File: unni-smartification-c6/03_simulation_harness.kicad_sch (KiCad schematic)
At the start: 10 parts

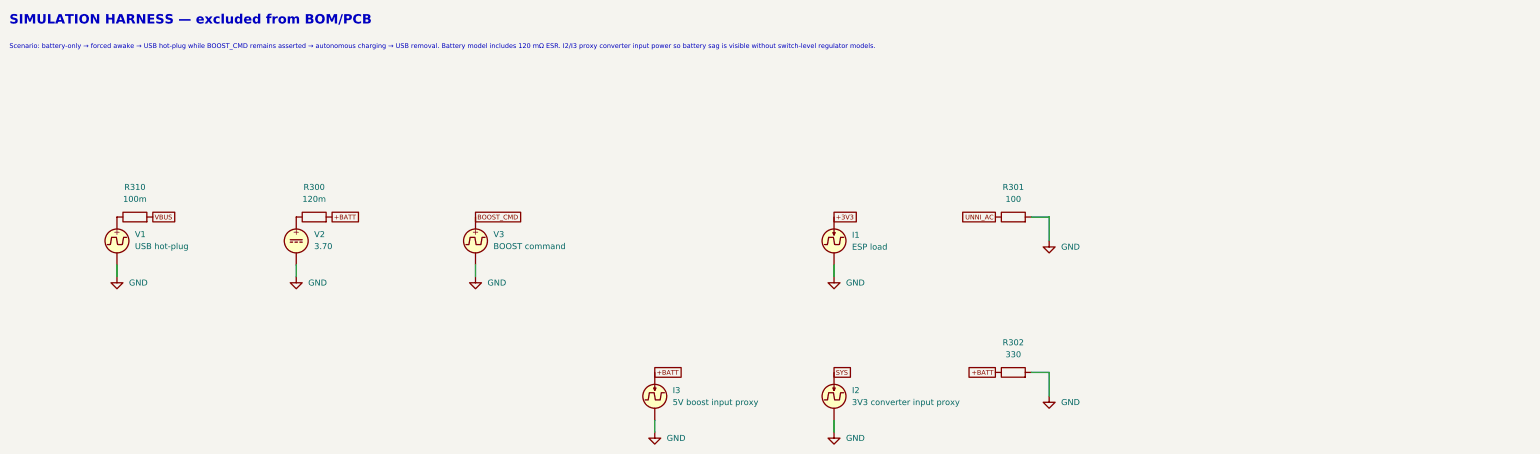
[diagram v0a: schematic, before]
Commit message: Validate power paths and fix KiCad SPICE models
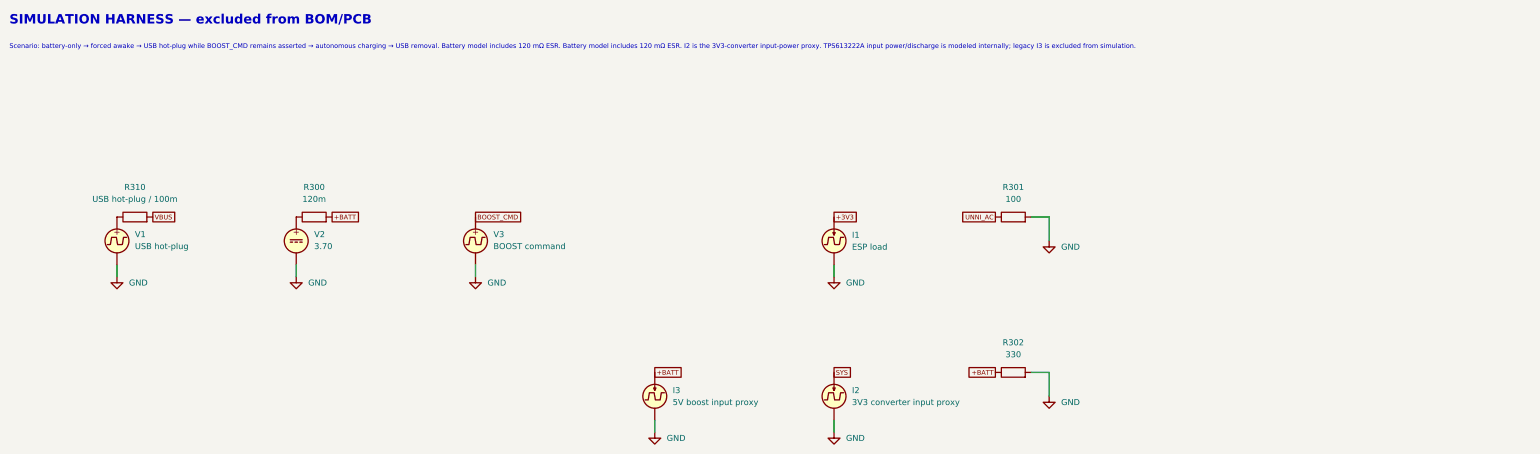
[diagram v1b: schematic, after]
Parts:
- R310: value 100m -> USB hot-plug / 100m
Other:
- note added: "Scenario: battery-only → forced awake → USB hot-plug while BOOST_CMD remains asserted → autonomous charging → USB removal. Battery model includes 120 mΩ ESR. Battery model includes 120 mΩ ESR. I2 is the 3V3-converter input-power proxy. TPS613222A input power/discharge is modeled internally; legacy I3 is excluded from simulation."
- note removed: "Scenario: battery-only → forced awake → USB hot-plug while BOOST_CMD remains asserted → autonomous charging → USB removal. Battery model includes 120 mΩ ESR. I2/I3 proxy converter input power so battery sag is visible without switch-level regulator models."
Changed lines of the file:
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@@
 		(title "Simulation Harness")
 		(date "2026-08-19")
-		(rev "A-v28-final")
+		(rev "A-v29-validated")
 		(company "Unni CO2 Smartification")
 	)
@@
 		)
 	)
-	(text "Scenario: battery-only → forced awake → USB hot-plug while BOOST_CMD remains asserted → autonomous charging → USB removal. Battery model includes 120 mΩ ESR. I2/I3 proxy converter input power so battery sag is visible without switch-level regulator models."
+	(text "Scenario: battery-only → forced awake → USB hot-plug while BOOST_CMD remains asserted → autonomous charging → USB removal. Battery model includes 120 mΩ ESR. Battery model includes 120 mΩ ESR. I2 is the 3V3-converter input-power proxy. TPS613222A input power/discharge is modeled internally; legacy I3 is excluded from simulation."
 		(exclude_from_sim no)
 		(at 15.24 20.32 0)
@@
 			)
 		)
-		(property "Value" "100m"
+		(property "Value" "USB hot-plug / 100m"
 			(at 41.91 52.07 90)
 			(show_name no)
@@
 			)
 		)
-		(property "Description" "USB source/cable resistance (simulation only)"
+		(property "Description" "USB hot-plug switch with 100m on-resistance (simulation only)"
 			(at 41.91 55.88 0)
 			(hide yes)
@@
 				)
 			)
+		)
+		(property "Sim.Library" "spice/models/USB_HOTPLUG.lib"
+			(at 41.91 55.88 0)
+			(hide yes)
+			(show_name no)
+			(do_not_autoplace no)
+			(effects (font (size 1 1)))
+		)
+		(property "Sim.Name" "USB_HOTPLUG"
+			(at 41.91 55.88 0)
+			(hide yes)
+			(show_name no)
+			(do_not_autoplace no)
+			(effects (font (size 1 1)))
+		)
+		(property "Sim.Pins" "1=1 2=2"
+			(at 41.91 55.88 0)
+			(hide yes)
+			(show_name no)
+			(do_not_autoplace no)
+			(effects (font (size 1 1)))
 		)
 		(pin "1"
@@
 		(unit 1)
 		(body_style 1)
-		(exclude_from_sim no)
+		(exclude_from_sim yes)
 		(in_bom no)
 		(on_board no)

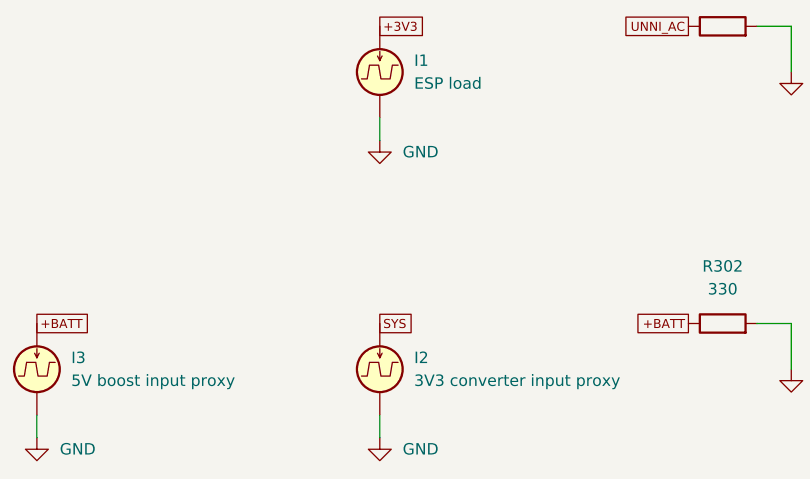
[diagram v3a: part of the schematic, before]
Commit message: trying routing the usb-pcb
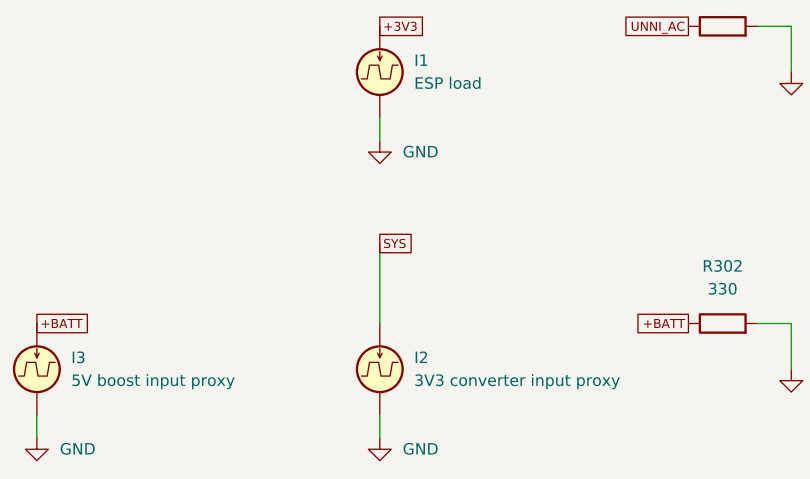
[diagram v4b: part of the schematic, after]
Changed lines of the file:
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@@
+	(wire
+		(pts
+			(xy 190.5 80.01) (xy 190.5 88.9)
+		)
+		(stroke
+			(width 0)
+			(type default)
+		)
+	)
 	(wire
 		(pts
@@
 	(global_label "SYS"
 		(shape passive)
-		(at 190.5 88.9 0)
+		(at 190.5 80.01 0)
 		(fields_autoplaced yes)
 		(effects
@@
 		)
 		(property "Intersheetrefs" "${INTERSHEET_REFS}"
-			(at 194.7372 88.9 0)
+			(at 194.7372 80.01 0)
 			(hide yes)
 			(show_name no)
@@
 		(in_pos_files yes)
 		(dnp no)
+		(passthrough block)
 		(fields_autoplaced yes)
 		(property "Reference" "I2"
